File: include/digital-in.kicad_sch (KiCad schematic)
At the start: 2 parts, among them U9 EL817

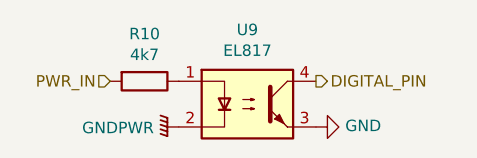
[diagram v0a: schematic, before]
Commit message: shrink resistor in digital-in
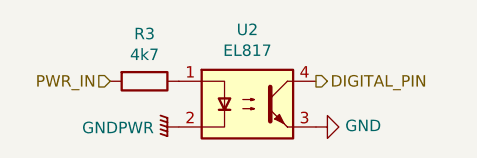
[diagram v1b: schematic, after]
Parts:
- R3: renamed from R10; footprint Resistor_SMD:R_0805_2012Metric -> Resistor_SMD:R_0402_1005Metric; LCSC C17673 -> C25117
- renumbered U9 to U2
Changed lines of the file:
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@@
   (symbol (lib_id "power:GNDPWR") (at 53.34 35.56 270)
     (in_bom yes) (on_board yes)
-    (property "Reference" "#PWR0115" (id 0) (at 48.26 35.56 0)
+    (property "Reference" "#PWR0101" (id 0) (at 48.26 35.56 0)
       (effects (font (size 1.27 1.27)) hide)
     )
@@
   (symbol (lib_id "power:GND") (at 68.58 35.56 90)
     (in_bom yes) (on_board yes)
-    (property "Reference" "#PWR0116" (id 0) (at 74.93 35.56 0)
+    (property "Reference" "#PWR0102" (id 0) (at 74.93 35.56 0)
       (effects (font (size 1.27 1.27)) hide)
     )
@@
   (symbol (lib_id "Device:R") (at 49.53 30.48 270)
     (in_bom yes) (on_board yes)
-    (property "Reference" "R10" (id 0) (at 49.53 25.2222 90))
+    (property "Reference" "R3" (id 0) (at 49.53 25.2222 90))
     (property "Value" "4k7" (id 1) (at 49.53 27.5336 90))
-    (property "Footprint" "Resistor_SMD:R_0805_2012Metric" (id 2) (at 49.53 28.702 90)
+    (property "Footprint" "Resistor_SMD:R_0402_1005Metric" (id 2) (at 49.53 28.702 90)
       (effects (font (size 1.27 1.27)) hide)
     )
-    (property "Datasheet" "~" (id 3) (at 49.53 30.48 0)
+    (property "Datasheet" "https://datasheet.lcsc.com/lcsc/1810170414_UNI-ROYAL-Uniroyal-Elec-0402WGF4700TCE_C25117.pdf" (id 3) (at 49.53 30.48 0)
       (effects (font (size 1.27 1.27)) hide)
     )
-    (property "LCSC" "C17673" (id 4) (at 49.53 30.48 90)
+    (property "LCSC" "C25117" (id 4) (at 49.53 30.48 90)
       (effects (font (size 1.27 1.27)) hide)
     )
@@
   (symbol (lib_id "jlcpcb:EL817") (at 60.96 33.02 0)
     (in_bom yes) (on_board yes)
-    (property "Reference" "U9" (id 0) (at 60.96 24.765 0))
+    (property "Reference" "U2" (id 0) (at 60.96 24.765 0))
     (property "Value" "EL817" (id 1) (at 60.96 27.0764 0))
     (property "Footprint" "jlcpcb:EL817" (id 2) (at 82.55 38.1 0)

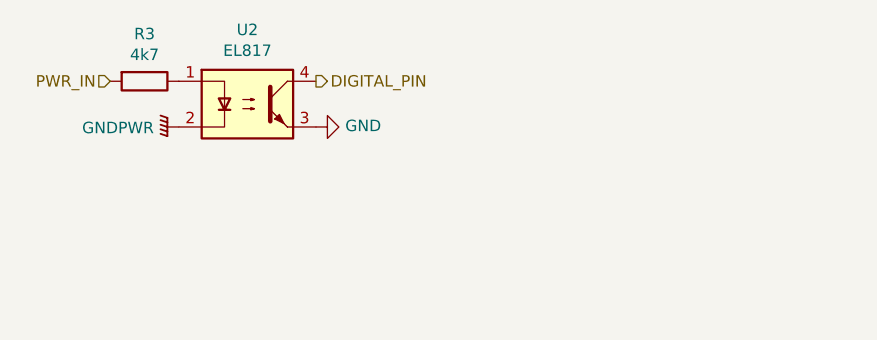
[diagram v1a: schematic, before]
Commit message: refactor slave-8in-8out
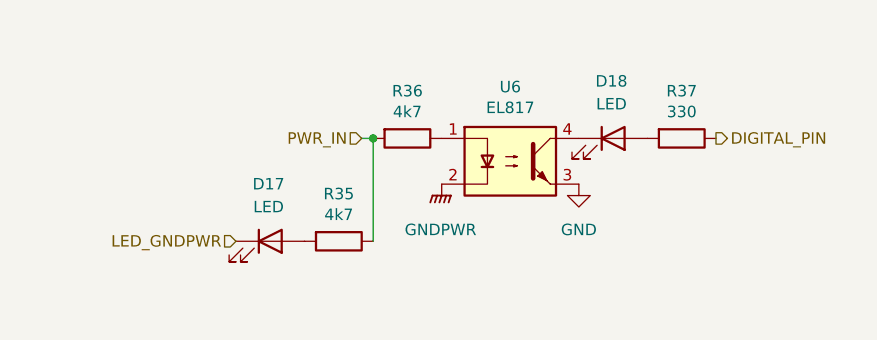
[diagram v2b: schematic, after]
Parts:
- removed R3: 4k7, Resistor_SMD:R_0402_1005Metric, symbol Device:R
- removed U2: EL817, jlcpcb:EL817, symbol jlcpcb:EL817
- added D17, D18: LED, Resistor_SMD:R_0805_2012Metric, symbol Device:LED
- added R35, R36: 4k7, Resistor_SMD:R_0805_2012Metric, symbol Device:R
- added R37: 330, Resistor_SMD:R_0402_1005Metric, symbol Device:R
- added U6: EL817, jlcpcb:EL817, symbol jlcpcb:EL817
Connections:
- net DIGITAL_PIN: now also R37.1
- net GND: now also U6.3
- net GNDPWR: now also U6.2
- net PWR_IN: now also R35.1, R36.2
- new net: D18.1 (K), U6.4
- new net: D18.2 (A), R37.2
- new net: R36.1, U6.1
- new net: D17.2 (A), R35.2
- new net LED_GNDPWR: D17.1 (K)
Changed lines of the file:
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@@
 (kicad_sch (version 20210621) (generator eeschema)
   (paper "A4")
-  (hierarchical_label "PWR_IN" (shape input) (at 45.72 30.48 180)
+  (junction (at 74.93 36.83) (diameter 0.9144) (color 0 0 0 0))
+  (wire (pts (xy 73.66 36.83) (xy 74.93 36.83))
+    (stroke (width 0) (type solid) (color 0 0 0 0))
+  )
+  (wire (pts (xy 74.93 36.83) (xy 74.93 48.26))
+    (stroke (width 0) (type solid) (color 0 0 0 0))
+  )
+  (hierarchical_label "LED_GNDPWR" (shape input) (at 59.69 48.26 180)
     (effects (font (size 1.27 1.27)) (justify right))
   )
-  (hierarchical_label "DIGITAL_PIN" (shape output) (at 68.58 30.48 0)
+  (hierarchical_label "PWR_IN" (shape input) (at 73.66 36.83 180)
+    (effects (font (size 1.27 1.27)) (justify right))
+  )
+  (hierarchical_label "DIGITAL_PIN" (shape output) (at 113.03 36.83 0)
     (effects (font (size 1.27 1.27)) (justify left))
   )
-  (symbol (lib_id "power:GNDPWR") (at 53.34 35.56 270)
-    (in_bom yes) (on_board yes)
-    (property "Reference" "#PWR0101" (id 0) (at 48.26 35.56 0)
+  (symbol (lib_id "power:GNDPWR") (at 82.55 41.91 0)
+    (in_bom yes) (on_board yes) (fields_autoplaced)
+    (property "Reference" "#PWR0109" (id 0) (at 82.55 46.99 0)
       (effects (font (size 1.27 1.27)) hide)
     )
-    (property "Value" "GNDPWR" (id 1) (at 50.5714 35.6616 90)
-      (effects (font (size 1.27 1.27)) (justify right))
-    )
-    (property "Footprint" "" (id 2) (at 52.07 35.56 0)
+    (property "Value" "GNDPWR" (id 1) (at 82.423 46.99 0))
+    (property "Footprint" "" (id 2) (at 82.55 43.18 0)
       (effects (font (size 1.27 1.27)) hide)
     )
-    (property "Datasheet" "" (id 3) (at 52.07 35.56 0)
+    (property "Datasheet" "" (id 3) (at 82.55 43.18 0)
       (effects (font (size 1.27 1.27)) hide)
     )
     (pin "1")
   )
-  (symbol (lib_id "power:GND") (at 68.58 35.56 90)
-    (in_bom yes) (on_board yes)
-    (property "Reference" "#PWR0102" (id 0) (at 74.93 35.56 0)
+  (symbol (lib_id "power:GND") (at 97.79 41.91 0)
+    (in_bom yes) (on_board yes) (fields_autoplaced)
+    (property "Reference" "#PWR0110" (id 0) (at 97.79 48.26 0)
       (effects (font (size 1.27 1.27)) hide)
     )
-    (property "Value" "GND" (id 1) (at 71.8312 35.433 90)
-      (effects (font (size 1.27 1.27)) (justify right))
-    )
-    (property "Footprint" "" (id 2) (at 68.58 35.56 0)
+    (property "Value" "GND" (id 1) (at 97.79 46.99 0))
+    (property "Footprint" "" (id 2) (at 97.79 41.91 0)
       (effects (font (size 1.27 1.27)) hide)
     )
-    (property "Datasheet" "" (id 3) (at 68.58 35.56 0)
+    (property "Datasheet" "" (id 3) (at 97.79 41.91 0)
       (effects (font (size 1.27 1.27)) hide)
     )
     (pin "1")
   )
-  (symbol (lib_id "Device:R") (at 49.53 30.48 270)
+  (symbol (lib_id "Device:R") (at 71.12 48.26 270)
     (in_bom yes) (on_board yes)
-    (property "Reference" "R3" (id 0) (at 49.53 25.2222 90))
-    (property "Value" "4k7" (id 1) (at 49.53 27.5336 90))
-    (property "Footprint" "Resistor_SMD:R_0402_1005Metric" (id 2) (at 49.53 28.702 90)
+    (property "Reference" "R35" (id 0) (at 71.12 43.0022 90))
+    (property "Value" "4k7" (id 1) (at 71.12 45.3136 90))
+    (property "Footprint" "Resistor_SMD:R_0805_2012Metric" (id 2) (at 71.12 46.482 90)
       (effects (font (size 1.27 1.27)) hide)
     )
-    (property "Datasheet" "https://datasheet.lcsc.com/lcsc/1810170414_UNI-ROYAL-Uniroyal-Elec-0402WGF4700TCE_C25117.pdf" (id 3) (at 49.53 30.48 0)
+    (property "Datasheet" "https://datasheet.lcsc.com/lcsc/1811050105_UNI-ROYAL-Uniroyal-Elec-0805W8F4700T5E_C17710.pdf" (id 3) (at 71.12 48.26 0)
       (effects (font (size 1.27 1.27)) hide)
     )
-    (property "LCSC" "C25117" (id 4) (at 49.53 30.48 90)
+    (property "LCSC" "C17710" (id 4) (at 71.12 48.26 90)
       (effects (font (size 1.27 1.27)) hide)
     )
@@
     (pin "2")
   )
-  (symbol (lib_id "jlcpcb:EL817") (at 60.96 33.02 0)
+  (symbol (lib_id "Device:R") (at 78.74 36.83 270)
     (in_bom yes) (on_board yes)
-    (property "Reference" "U2" (id 0) (at 60.96 24.765 0))
-    (property "Value" "EL817" (id 1) (at 60.96 27.0764 0))
-    (property "Footprint" "jlcpcb:EL817" (id 2) (at 82.55 38.1 0)
+    (property "Reference" "R36" (id 0) (at 78.74 31.5722 90))
+    (property "Value" "4k7" (id 1) (at 78.74 33.8836 90))
+    (property "Footprint" "Resistor_SMD:R_0805_2012Metric" (id 2) (at 78.74 35.052 90)
       (effects (font (size 1.27 1.27)) hide)
     )
-    (property "Datasheet" "https://datasheet.lcsc.com/szlcsc/Everlight-Elec-EL817S1-C-TU-F_C106900.pdf" (id 3) (at 60.96 33.02 0)
+    (property "Datasheet" "https://datasheet.lcsc.com/lcsc/1811050105_UNI-ROYAL-Uniroyal-Elec-0805W8F4700T5E_C17710.pdf" (id 3) (at 78.74 36.83 0)
       (effects (font (size 1.27 1.27)) hide)
     )
-    (property "LCSC" "C106900" (id 4) (at 55.88 38.1 0)
+    (property "LCSC" "C17710" (id 4) (at 78.74 36.83 90)
       (effects (font (size 1.27 1.27)) hide)
     )
+    (pin "1")
+    (pin "2")
+  )
+  (symbol (lib_id "Device:R") (at 109.22 36.83 270)
+    (in_bom yes) (on_board yes)
+    (property "Reference" "R37" (id 0) (at 109.22 31.5722 90))
+    (property "Value" "330" (id 1) (at 109.22 33.8836 90))
+    (property "Footprint" "Resistor_SMD:R_0402_1005Metric" (id 2) (at 109.22 35.052 90)
+      (effects (font (size 1.27 1.27)) hide)
+    )
+    (property "Datasheet" "https://datasheet.lcsc.com/lcsc/1810170414_UNI-ROYAL-Uniroyal-Elec-0402WGF4700TCE_C25117.pdf" (id 3) (at 109.22 36.83 0)
+      (effects (font (size 1.27 1.27)) hide)
+    )
+    (property "LCSC" "C25117" (id 4) (at 109.22 36.83 90)
+      (effects (font (size 1.27 1.27)) hide)
+    )
+    (pin "1")
+    (pin "2")
+  )
+  (symbol (lib_id "Device:LED") (at 63.5 48.26 0)
+    (in_bom yes) (on_board yes) (fields_autoplaced)
+    (property "Reference" "D17" (id 0) (at 63.3095 41.91 0))
+    (property "Value" "LED" (id 1) (at 63.3095 44.45 0))
+    (property "Footprint" "Resistor_SMD:R_0805_2012Metric" (id 2) (at 63.5 48.26 0)
+      (effects (font (size 1.27 1.27)) hide)
+    )
+    (property "Datasheet" "https://datasheet.lcsc.com/lcsc/2008201032_Foshan-NationStar-Optoelectronics-NCD0805R1_C84256.pdf" (id 3) (at 63.5 48.26 0)
+      (effects (font (size 1.27 1.27)) hide)
+    )
+    (property "LCSC" "C84256" (id 4) (at 63.5 48.26 0)
+      (effects (font (size 1.27 1.27)) hide)
+    )
+    (pin "1")
+    (pin "2")
+  )
+  (symbol (lib_id "Device:LED") (at 101.6 36.83 0)
+    (in_bom yes) (on_board yes) (fields_autoplaced)
+    (property "Reference" "D18" (id 0) (at 101.4095 30.48 0))
+    (property "Value" "LED" (id 1) (at 101.4095 33.02 0))
+    (property "Footprint" "Resistor_SMD:R_0805_2012Metric" (id 2) (at 101.6 36.83 0)
+      (effects (font (size 1.27 1.27)) hide)
+    )
+    (property "Datasheet" "https://datasheet.lcsc.com/lcsc/2008201032_Foshan-NationStar-Optoelectronics-NCD0805R1_C84256.pdf" (id 3) (at 101.6 36.83 0)
+      (effects (font (size 1.27 1.27)) hide)
+    )
+    (property "LCSC" "C84256" (id 4) (at 101.6 36.83 0)
+      (effects (font (size 1.27 1.27)) hide)
+    )
+    (pin "1")
+    (pin "2")
+  )
+  (symbol (lib_id "jlcpcb:EL817") (at 90.17 39.37 0)
+    (in_bom yes) (on_board yes)
+    (property "Reference" "U6" (id 0) (at 90.17 31.115 0))
+    (property "Value" "EL817" (id 1) (at 90.17 33.4264 0))
+    (property "Footprint" "jlcpcb:EL817" (id 2) (at 111.76 44.45 0)
+      (effects (font (size 1.27 1.27)) hide)
+    )
+    (property "Datasheet" "https://datasheet.lcsc.com/szlcsc/Everlight-Elec-EL817S1-C-TU-F_C106900.pdf" (id 3) (at 90.17 39.37 0)
+      (effects (font (size 1.27 1.27)) hide)
+    )
+    (property "LCSC" "C106900" (id 4) (at 85.09 44.45 0)
+      (effects (font (size 1.27 1.27)) hide)
+    )

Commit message: refactor slave-8in-8out
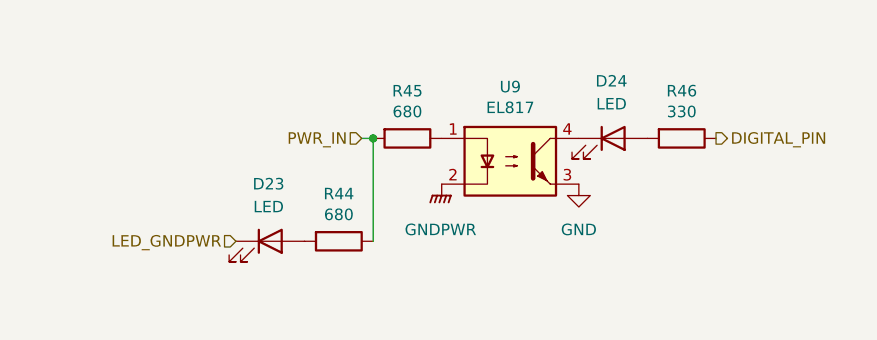
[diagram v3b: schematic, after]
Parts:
- removed R35: 4k7, Resistor_SMD:R_0805_2012Metric, symbol Device:R
- added R44: 680, Resistor_SMD:R_0402_1005Metric, symbol Device:R
- R45: renamed from R36; value 4k7 -> 680; footprint Resistor_SMD:R_0805_2012Metric -> Resistor_SMD:R_0402_1005Metric; LCSC C17710 -> C25917
- renumbered D17 to D23, D18 to D24, R37 to R46, U6 to U9
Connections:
- net PWR_IN: now also R44.1
- net at D23.2 (A): now also R44.2
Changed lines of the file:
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@@
   (symbol (lib_id "power:GNDPWR") (at 82.55 41.91 0)
     (in_bom yes) (on_board yes) (fields_autoplaced)
-    (property "Reference" "#PWR0109" (id 0) (at 82.55 46.99 0)
+    (property "Reference" "#PWR0115" (id 0) (at 82.55 46.99 0)
       (effects (font (size 1.27 1.27)) hide)
     )
@@
   (symbol (lib_id "power:GND") (at 97.79 41.91 0)
     (in_bom yes) (on_board yes) (fields_autoplaced)
-    (property "Reference" "#PWR0110" (id 0) (at 97.79 48.26 0)
+    (property "Reference" "#PWR0116" (id 0) (at 97.79 48.26 0)
       (effects (font (size 1.27 1.27)) hide)
     )
@@
   (symbol (lib_id "Device:R") (at 71.12 48.26 270)
     (in_bom yes) (on_board yes)
-    (property "Reference" "R35" (id 0) (at 71.12 43.0022 90))
-    (property "Value" "4k7" (id 1) (at 71.12 45.3136 90))
-    (property "Footprint" "Resistor_SMD:R_0805_2012Metric" (id 2) (at 71.12 46.482 90)
+    (property "Reference" "R44" (id 0) (at 71.12 43.0022 90))
+    (property "Value" "680" (id 1) (at 71.12 45.3136 90))
+    (property "Footprint" "Resistor_SMD:R_0402_1005Metric" (id 2) (at 71.12 46.482 90)
       (effects (font (size 1.27 1.27)) hide)
     )
-    (property "Datasheet" "https://datasheet.lcsc.com/lcsc/1811050105_UNI-ROYAL-Uniroyal-Elec-0805W8F4700T5E_C17710.pdf" (id 3) (at 71.12 48.26 0)
+    (property "Datasheet" "https://datasheet.lcsc.com/lcsc/1811011222_UNI-ROYAL-Uniroyal-Elec-0402WGF6801TCE_C25917.pdf" (id 3) (at 71.12 48.26 0)
       (effects (font (size 1.27 1.27)) hide)
     )
-    (property "LCSC" "C17710" (id 4) (at 71.12 48.26 90)
+    (property "LCSC" "C25917" (id 4) (at 71.12 48.26 90)
       (effects (font (size 1.27 1.27)) hide)
     )
@@
   (symbol (lib_id "Device:R") (at 78.74 36.83 270)
     (in_bom yes) (on_board yes)
-    (property "Reference" "R36" (id 0) (at 78.74 31.5722 90))
-    (property "Value" "4k7" (id 1) (at 78.74 33.8836 90))
-    (property "Footprint" "Resistor_SMD:R_0805_2012Metric" (id 2) (at 78.74 35.052 90)
+    (property "Reference" "R45" (id 0) (at 78.74 31.5722 90))
+    (property "Value" "680" (id 1) (at 78.74 33.8836 90))
+    (property "Footprint" "Resistor_SMD:R_0402_1005Metric" (id 2) (at 78.74 35.052 90)
       (effects (font (size 1.27 1.27)) hide)
     )
-    (property "Datasheet" "https://datasheet.lcsc.com/lcsc/1811050105_UNI-ROYAL-Uniroyal-Elec-0805W8F4700T5E_C17710.pdf" (id 3) (at 78.74 36.83 0)
+    (property "Datasheet" "https://datasheet.lcsc.com/lcsc/1811011222_UNI-ROYAL-Uniroyal-Elec-0402WGF6801TCE_C25917.pdf" (id 3) (at 78.74 36.83 0)
       (effects (font (size 1.27 1.27)) hide)
     )
-    (property "LCSC" "C17710" (id 4) (at 78.74 36.83 90)
+    (property "LCSC" "C25917" (id 4) (at 78.74 36.83 90)
       (effects (font (size 1.27 1.27)) hide)
     )
@@
   (symbol (lib_id "Device:R") (at 109.22 36.83 270)
     (in_bom yes) (on_board yes)
-    (property "Reference" "R37" (id 0) (at 109.22 31.5722 90))
+    (property "Reference" "R46" (id 0) (at 109.22 31.5722 90))
     (property "Value" "330" (id 1) (at 109.22 33.8836 90))
     (property "Footprint" "Resistor_SMD:R_0402_1005Metric" (id 2) (at 109.22 35.052 90)
@@
   (symbol (lib_id "Device:LED") (at 63.5 48.26 0)
     (in_bom yes) (on_board yes) (fields_autoplaced)
-    (property "Reference" "D17" (id 0) (at 63.3095 41.91 0))
+    (property "Reference" "D23" (id 0) (at 63.3095 41.91 0))
     (property "Value" "LED" (id 1) (at 63.3095 44.45 0))
     (property "Footprint" "Resistor_SMD:R_0805_2012Metric" (id 2) (at 63.5 48.26 0)
@@
   (symbol (lib_id "Device:LED") (at 101.6 36.83 0)
     (in_bom yes) (on_board yes) (fields_autoplaced)
-    (property "Reference" "D18" (id 0) (at 101.4095 30.48 0))
+    (property "Reference" "D24" (id 0) (at 101.4095 30.48 0))
     (property "Value" "LED" (id 1) (at 101.4095 33.02 0))
     (property "Footprint" "Resistor_SMD:R_0805_2012Metric" (id 2) (at 101.6 36.83 0)
@@
   (symbol (lib_id "jlcpcb:EL817") (at 90.17 39.37 0)
     (in_bom yes) (on_board yes)
-    (property "Reference" "U6" (id 0) (at 90.17 31.115 0))
+    (property "Reference" "U9" (id 0) (at 90.17 31.115 0))
     (property "Value" "EL817" (id 1) (at 90.17 33.4264 0))
     (property "Footprint" "jlcpcb:EL817" (id 2) (at 111.76 44.45 0)
